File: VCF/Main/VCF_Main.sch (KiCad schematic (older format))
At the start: 51 parts, among them J1 Input, J2 Power, J4 RES_MOD, J5 FREQ_CV, J6 AUDIO_OUT, U1 TL072, U2 TL072, U3 AS3320

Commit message: Update VCF main board for new front panel
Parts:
- removed C1: 15uF, Capacitor_SMD:C_0805_2012Metric, symbol Device:C
- removed C6: 1uF, Capacitor_SMD:C_0805_2012Metric, symbol Device:C
- removed J1: Input, Connector_PinHeader_2.54mm:PinHeader_1x04_P2.54mm_Vertical, symbol Connector_Generic:Conn_01x04
- removed J4: RES_MOD, Connector_PinHeader_2.54mm:PinHeader_1x02_P2.54mm_Vertical, symbol Connector_Generic:Conn_01x02
- removed J5: FREQ_CV, Connector_PinHeader_2.54mm:PinHeader_1x02_P2.54mm_Vertical, symbol Connector_Generic:Conn_01x02
- removed J6: AUDIO_OUT, Connector_PinHeader_2.54mm:PinHeader_1x02_P2.54mm_Vertical, symbol Connector_Generic:Conn_01x02
- removed RV4, RV5: 100K, Connector_PinHeader_2.54mm:PinHeader_1x03_P2.54mm_Vertical, symbol Device:R_POT_US
- added C1: 15uF, Capacitor_SMD:CP_Elec_4x3, symbol Device:CP1
- added C6: 1uF, Capacitor_SMD:CP_Elec_4x3, symbol Device:CP1
- added J1: Power, Connector_PinHeader_2.54mm:PinHeader_1x12_P2.54mm_Vertical, symbol Connector_Generic:Conn_01x12
- C2, C3, C4, C5: footprint AS3320_VCF:Mica_Cap -> Eurorack:Mica_Cap
- R26: footprint AS3320_VCF:Tempco -> Eurorack:Tempco
- U3: symbol AS3320_VCF:AS3320 -> Eurorack:AS3320
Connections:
- net +12V: now also J1.2 (Pin_2)
- net -12V: now also J1.3 (Pin_3)
- net GNDREF: now also J1.1 (Pin_1), J1.12 (Pin_12)
- net at R22.1, U3.10: now also C6.1
- net at R5.2: now also C1.1
- net at R25.2, R27.2: now also C6.2
- net Cutoff_Mod: now reaches R17.2
- net Cutoff_Mod: now also J1.7 (Pin_7)
- net In_1: now reaches R1.2
- net In_1: now also J1.8 (Pin_8)
- net In_2: now reaches R2.2
- net In_2: now also J1.9 (Pin_9)
- net In_3: now reaches R3.2
- net In_3: now also J1.10 (Pin_10)
- net Cutoff: now reaches R15.2
- net Cutoff: now also J1.6 (Pin_6)
- net Res: now reaches R11.2
- net Res: now also J1.4 (Pin_4)
- net Res_Mod: now reaches R12.2
- net Res_Mod: now also J1.5 (Pin_5)
- net at R4.1, U1.7: now also C1.2
- net Out: now reaches R30.1
- net Out: now also J1.11 (Pin_11)
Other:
- moved on the sheet: R1, R12, R3

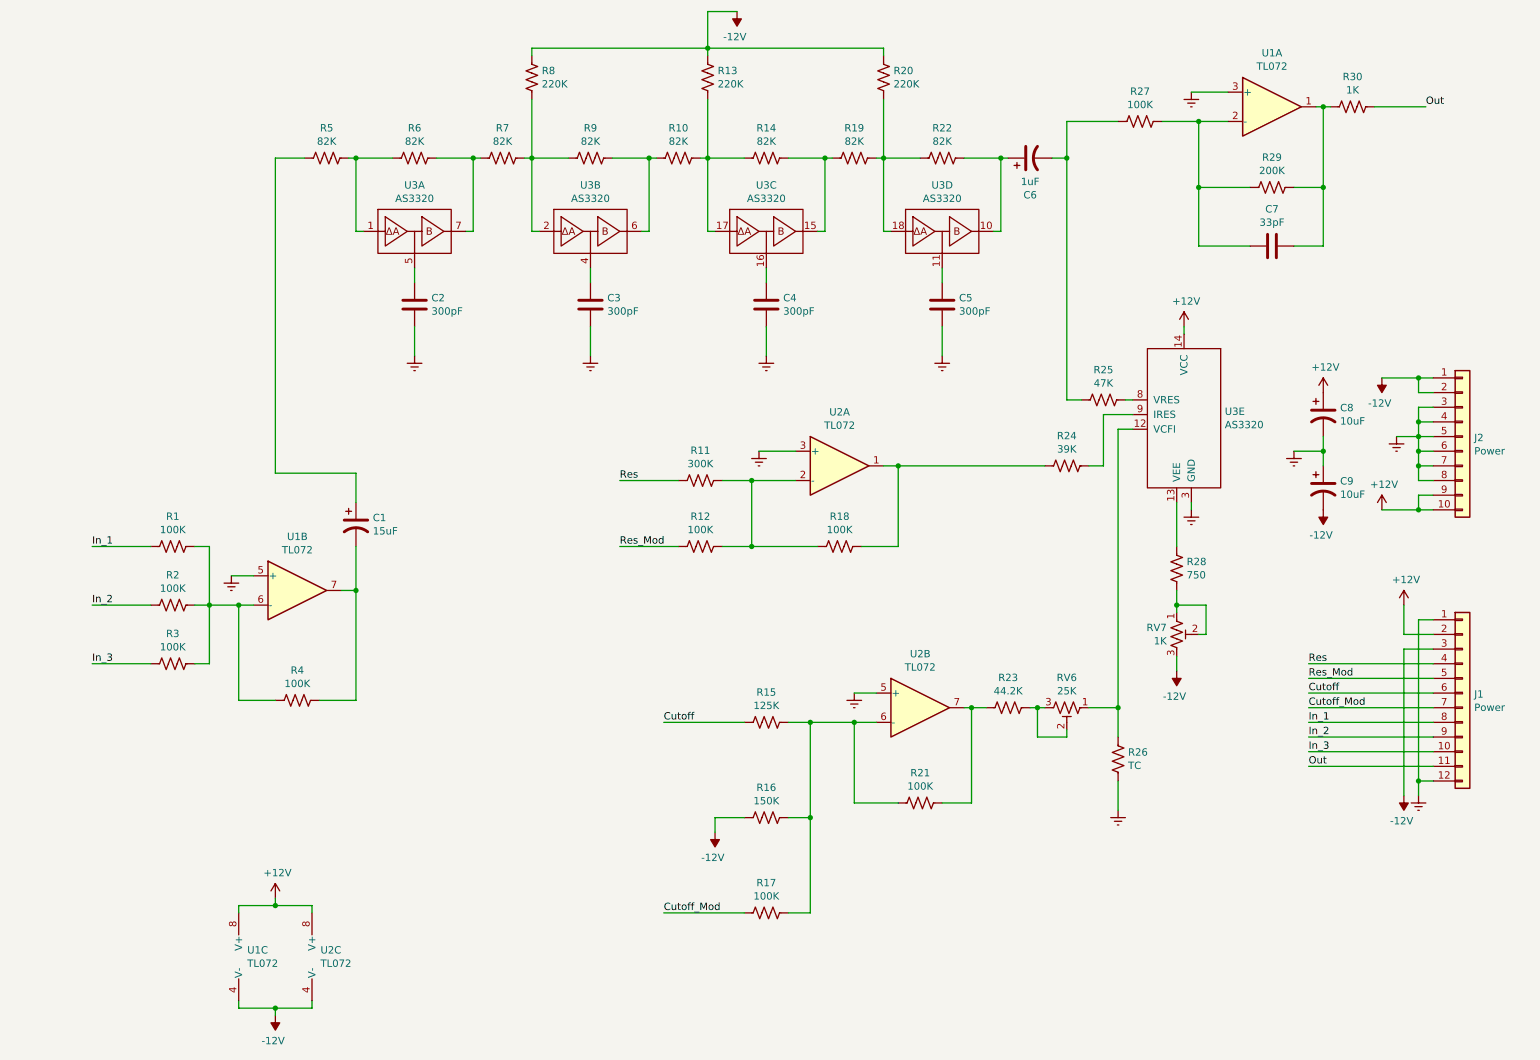
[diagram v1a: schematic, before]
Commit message: Fix inverted resonance control input
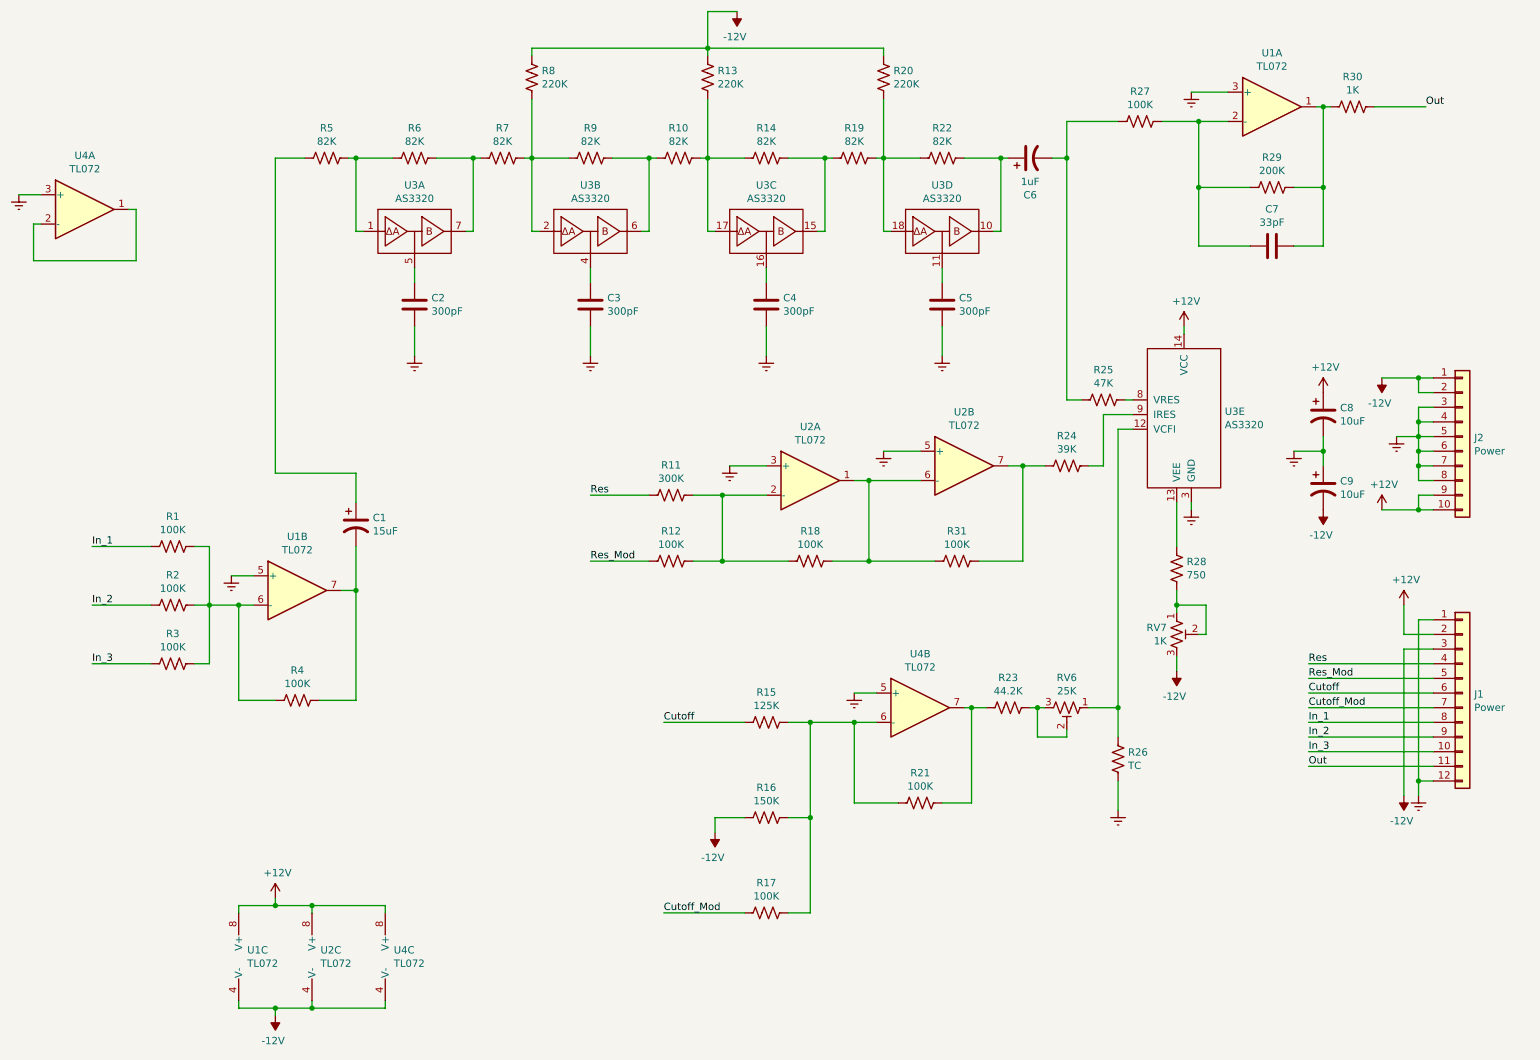
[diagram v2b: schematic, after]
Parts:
- added R31: 100K, Resistor_SMD:R_0805_2012Metric, symbol Device:R_US
- added U4: TL072, Package_DIP:DIP-8_W7.62mm, symbol Amplifier_Operational:TL072
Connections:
- net +12V: now also U4.8 (V+)
- net -12V: now also U4.4 (V-)
- net GNDREF: now also U4.3 (+), U4.5 (+)
- net at R18.1, U2.1: now also U2.6 (-), R31.2; no longer R24.2
- net at R15.1, R16.1, R17.1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: now also U4.6 (-); no longer U2.6 (-)
- net at R21.1, R23.2: now also U4.7; no longer U2.7
- new net: R24.2, R31.1, U2.7
- new net: U4.1, U4.2 (-)
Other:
- moved on the sheet: R11, R12, R18, U2A, U2B
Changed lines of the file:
@@
 L Amplifier_Operational:TL072 U2
 U 1 1 5D5A693C
-P 6450 3650
-F 0 "U2" H 6450 4017 50  0000 C CNN
-F 1 "TL072" H 6450 3926 50  0000 C CNN
-F 2 "Package_DIP:DIP-8_W7.62mm" H 6450 3650 50  0001 C CNN
-F 3 "http://www.ti.com/lit/ds/symlink/tl071.pdf" H 6450 3650 50  0001 C CNN
-	1    6450 3650
+P 6250 3750
+F 0 "U2" H 6250 4117 50  0000 C CNN
+F 1 "TL072" H 6250 4026 50  0000 C CNN
+F 2 "Package_DIP:DIP-8_W7.62mm" H 6250 3750 50  0001 C CNN
+F 3 "http://www.ti.com/lit/ds/symlink/tl071.pdf" H 6250 3750 50  0001 C CNN
+	1    6250 3750
 	1    0    0    -1
 $EndComp
@@
 L Amplifier_Operational:TL072 U2
 U 2 1 5D5A8C75
-P 7000 5300
-F 0 "U2" H 7000 5667 50  0000 C CNN
-F 1 "TL072" H 7000 5576 50  0000 C CNN
-F 2 "Package_DIP:DIP-8_W7.62mm" H 7000 5300 50  0001 C CNN
-F 3 "http://www.ti.com/lit/ds/symlink/tl071.pdf" H 7000 5300 50  0001 C CNN
-	2    7000 5300
+P 7300 3650
+F 0 "U2" H 7300 4017 50  0000 C CNN
+F 1 "TL072" H 7300 3926 50  0000 C CNN
+F 2 "Package_DIP:DIP-8_W7.62mm" H 7300 3650 50  0001 C CNN
+F 3 "http://www.ti.com/lit/ds/symlink/tl071.pdf" H 7300 3650 50  0001 C CNN
+	2    7300 3650
 	1    0    0    -1
 $EndComp
@@
 L power:GNDREF #PWR0118
 U 1 1 5D6384AF
-P 5900 3550
-F 0 "#PWR0118" H 5900 3300 50  0001 C CNN
-F 1 "GNDREF" H 5905 3377 50  0001 C CNN
-F 2 "" H 5900 3550 50  0001 C CNN
-F 3 "" H 5900 3550 50  0001 C CNN
-	1    5900 3550
-	1    0    0    -1
-$EndComp
-Wire Wire Line
-	5900 3550 6150 3550
+P 5700 3650
+F 0 "#PWR0118" H 5700 3400 50  0001 C CNN
+F 1 "GNDREF" H 5705 3477 50  0001 C CNN
+F 2 "" H 5700 3650 50  0001 C CNN
+F 3 "" H 5700 3650 50  0001 C CNN
+	1    5700 3650
+	1    0    0    -1
+$EndComp
+Wire Wire Line
+	5700 3650 5950 3650
 $Comp
 L Device:R_US R11
 U 1 1 5D647527
-P 5500 3750
-F 0 "R11" V 5295 3750 50  0000 C CNN
-F 1 "300K" V 5386 3750 50  0000 C CNN
-F 2 "Resistor_SMD:R_0805_2012Metric" V 5540 3740 50  0001 C CNN
-F 3 "~" H 5500 3750 50  0001 C CNN
-	1    5500 3750
+P 5300 3850
+F 0 "R11" V 5095 3850 50  0000 C CNN
+F 1 "300K" V 5186 3850 50  0000 C CNN
+F 2 "Resistor_SMD:R_0805_2012Metric" V 5340 3840 50  0001 C CNN
+F 3 "~" H 5300 3850 50  0001 C CNN
+	1    5300 3850
 	0    1    1    0
 $EndComp
@@
 L Device:R_US R12
 U 1 1 5D647C16
-P 5500 4200
-F 0 "R12" V 5295 4200 50  0000 C CNN
-F 1 "100K" V 5386 4200 50  0000 C CNN
-F 2 "Resistor_SMD:R_0805_2012Metric" V 5540 4190 50  0001 C CNN
-F 3 "~" H 5500 4200 50  0001 C CNN
-	1    5500 4200
+P 5300 4300
+F 0 "R12" V 5095 4300 50  0000 C CNN
+F 1 "100K" V 5186 4300 50  0000 C CNN
+F 2 "Resistor_SMD:R_0805_2012Metric" V 5340 4290 50  0001 C CNN
+F 3 "~" H 5300 4300 50  0001 C CNN
+	1    5300 4300
 	0    1    1    0
 $EndComp
@@
 L Device:R_US R18
 U 1 1 5D6482AE
-P 6450 4200
-F 0 "R18" V 6245 4200 50  0000 C CNN
-F 1 "100K" V 6336 4200 50  0000 C CNN
-F 2 "Resistor_SMD:R_0805_2012Metric" V 6490 4190 50  0001 C CNN
-F 3 "~" H 6450 4200 50  0001 C CNN
-	1    6450 4200
-	0    1    1    0
-$EndComp
-Wire Wire Line
-	4950 3750 5350 3750
-Wire Wire Line
-	5650 3750 5850 3750
-Wire Wire Line
-	4950 4200 5350 4200
-Wire Wire Line
-	5650 4200 5850 4200
-Connection ~ 5850 3750
-Wire Wire Line
-	5850 3750 6150 3750
-Wire Wire Line
-	5850 4200 6300 4200
-Connection ~ 5850 4200
-Wire Wire Line
-	5850 4200 5850 3750
-Wire Wire Line
-	6600 4200 6850 4200
-Wire Wire Line
-	6850 4200 6850 3650
-Wire Wire Line
-	6850 3650 6750 3650
-Connection ~ 6850 3650
+P 6250 4300
+F 0 "R18" V 6045 4300 50  0000 C CNN
+F 1 "100K" V 6136 4300 50  0000 C CNN
+F 2 "Resistor_SMD:R_0805_2012Metric" V 6290 4290 50  0001 C CNN
+F 3 "~" H 6250 4300 50  0001 C CNN
+	1    6250 4300
+	0    1    1    0
+$EndComp
+Wire Wire Line
+	4750 3850 5150 3850
+Wire Wire Line
+	5450 3850 5650 3850
+Wire Wire Line
+	4750 4300 5150 4300
+Wire Wire Line
+	5450 4300 5650 4300
+Connection ~ 5650 3850
+Wire Wire Line
+	5650 3850 5950 3850
+Wire Wire Line
+	5650 4300 6100 4300
+Connection ~ 5650 4300
+Wire Wire Line
+	5650 4300 5650 3850
+Wire Wire Line
+	6400 4300 6650 4300
+Wire Wire Line
+	6650 4300 6650 3750
+Wire Wire Line
+	6650 3750 6550 3750
+Connection ~ 6650 3750
 $Comp
 L Amplifier_Operational:TL072 U1
@@
 Connection ~ 8350 5300
 Wire Wire Line
-	6850 3650 7850 3650
+	6650 3750 7000 3750
 Wire Wire Line
 	2800 1550 2600 1550
@@
 Text Label 1350 5000 0    50   ~ 0
 In_3
-Text Label 4950 3750 0    50   ~ 0
+Text Label 4750 3850 0    50   ~ 0
 Res
-Text Label 4950 4200 0    50   ~ 0
+Text Label 4750 4300 0    50   ~ 0
 Res_Mod
 Text Label 5250 5400 0    50   ~ 0
@@
 	1    0    0    -1
 $EndComp
+$Comp
+L Amplifier_Operational:TL072 U4
+U 1 1 5D8DED88
+P 1300 1900
+F 0 "U4" H 1300 2267 50  0000 C CNN
+F 1 "TL072" H 1300 2176 50  0000 C CNN
+F 2 "Package_DIP:DIP-8_W7.62mm" H 1300 1900 50  0001 C CNN
+F 3 "http://www.ti.com/lit/ds/symlink/tl071.pdf" H 1300 1900 50  0001 C CNN
+	1    1300 1900
+	1    0    0    -1
+$EndComp
+$Comp
+L Amplifier_Operational:TL072 U4
+U 2 1 5D8E0532
+P 7000 5300
+F 0 "U4" H 7000 5667 50  0000 C CNN
+F 1 "TL072" H 7000 5576 50  0000 C CNN
+F 2 "Package_DIP:DIP-8_W7.62mm" H 7000 5300 50  0001 C CNN
+F 3 "http://www.ti.com/lit/ds/symlink/tl071.pdf" H 7000 5300 50  0001 C CNN
+	2    7000 5300
+	1    0    0    -1
+$EndComp
+$Comp
+L Amplifier_Operational:TL072 U4
+U 3 1 5D8E37FF
+P 3450 7000
+F 0 "U4" H 3408 7046 50  0000 L CNN
+F 1 "TL072" H 3408 6955 50  0000 L CNN
+F 2 "Package_DIP:DIP-8_W7.62mm" H 3450 7000 50  0001 C CNN
+F 3 "http://www.ti.com/lit/ds/symlink/tl071.pdf" H 3450 7000 50  0001 C CNN
+	3    3450 7000
+	1    0    0    -1
+$EndComp
+$Comp
+L Device:R_US R31
+U 1 1 5D93C727
+P 7250 4300
+F 0 "R31" V 7045 4300 50  0000 C CNN
+F 1 "100K" V 7136 4300 50  0000 C CNN
+F 2 "Resistor_SMD:R_0805_2012Metric" V 7290 4290 50  0001 C CNN
+F 3 "~" H 7250 4300 50  0001 C CNN
+	1    7250 4300
+	0    1    1    0
+$EndComp
+Wire Wire Line
+	6650 4300 7100 4300
+Connection ~ 6650 4300
+Wire Wire Line
+	7600 3650 7700 3650
+Wire Wire Line
+	7700 3650 7700 4300
+Wire Wire Line
+	7700 4300 7400 4300
+$Comp
+L power:GNDREF #PWR0110
+U 1 1 5D953B55
+P 6750 3550
+F 0 "#PWR0110" H 6750 3300 50  0001 C CNN
+F 1 "GNDREF" H 6755 3377 50  0001 C CNN
+F 2 "" H 6750 3550 50  0001 C CNN
+F 3 "" H 6750 3550 50  0001 C CNN
+	1    6750 3550
+	1    0    0    -1
+$EndComp
+Wire Wire Line
+	6750 3550 7000 3550
+Wire Wire Line
+	7700 3650 7850 3650
+Connection ~ 7700 3650
+$Comp
+L power:GNDREF #PWR0111
+U 1 1 5D9ABD29
+P 850 1800
+F 0 "#PWR0111" H 850 1550 50  0001 C CNN
+F 1 "GNDREF" H 855 1627 50  0001 C CNN
+F 2 "" H 850 1800 50  0001 C CNN
+F 3 "" H 850 1800 50  0001 C CNN
+	1    850  1800
+	1    0    0    -1
+$EndComp
+Wire Wire Line
+	850  1800 1000 1800
+Wire Wire Line
+	1000 2000 950  2000
+Wire Wire Line
+	950  2000 950  2250
+Wire Wire Line
+	950  2250 1650 2250
+Wire Wire Line
+	1650 2250 1650 1900
+Wire Wire Line
+	1650 1900 1600 1900
+Wire Wire Line
+	2850 6650 3350 6650
+Wire Wire Line
+	3350 6650 3350 6700
+Connection ~ 2850 6650
+Wire Wire Line
+	2850 7350 3350 7350
+Wire Wire Line
+	3350 7350 3350 7300
+Connection ~ 2850 7350
 $EndSCHEMATC

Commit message: Bunch of bug fixes and tweaks
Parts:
- added C10, C11, C12, C13: C, Capacitor_SMD:C_0805_2012Metric, symbol Device:C
- added H1: Top_MH1, Eurorack:eurorack_mounting_hole, symbol Mechanical:MountingHole_Pad
- added H2: Bottom_MH1, Eurorack:eurorack_mounting_hole, symbol Mechanical:MountingHole_Pad
- added H3: Top_MH2, Eurorack:eurorack_mounting_hole, symbol Mechanical:MountingHole_Pad
- added H4: Bottom_MH2, Eurorack:eurorack_mounting_hole, symbol Mechanical:MountingHole_Pad
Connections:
- net GNDREF: now also H1.1, H2.1, H3.1, H4.1
- net at R24.2, R31.1, U2.7: now also C13.2
- net at R15.1, R16.1, R17.1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: now also C12.1
- net at R21.1, R23.2, U4.7: now also C12.2
- net at R18.1, R31.2, U2.1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: now also C11.2, C13.1
- net at R11.1, R12.1, R18.2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: now also C11.1
- net at R1.1, R2.1, R3.1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: now also C10.1
- net at C1.2, R4.1, U1.7: now also C10.2
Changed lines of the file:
@@
 	3350 7350 3350 7300
 Connection ~ 2850 7350
+$Comp
+L Device:C C10
+U 1 1 5D939BB0
+P 2750 5700
+F 0 "C10" V 3002 5700 50  0000 C CNN
+F 1 "C" V 2911 5700 50  0000 C CNN
+F 2 "Capacitor_SMD:C_0805_2012Metric" H 2788 5550 50  0001 C CNN
+F 3 "~" H 2750 5700 50  0001 C CNN
+	1    2750 5700
+	0    -1   -1   0
+$EndComp
+Wire Wire Line
+	2350 5250 2350 5700
+Wire Wire Line
+	2350 5700 2600 5700
+Connection ~ 2350 5250
+Wire Wire Line
+	3150 5250 3150 5700
+Wire Wire Line
+	3150 5700 2900 5700
+Connection ~ 3150 5250
+$Comp
+L Device:C C11
+U 1 1 5D954A6E
+P 6250 4750
+F 0 "C11" V 6502 4750 50  0000 C CNN
+F 1 "C" V 6411 4750 50  0000 C CNN
+F 2 "Capacitor_SMD:C_0805_2012Metric" H 6288 4600 50  0001 C CNN
+F 3 "~" H 6250 4750 50  0001 C CNN
+	1    6250 4750
+	0    -1   -1   0
+$EndComp
+Wire Wire Line
+	5650 4300 5650 4750
+Wire Wire Line
+	5650 4750 6100 4750
+Wire Wire Line
+	6400 4750 6650 4750
+Wire Wire Line
+	6650 4750 6650 4300
+$Comp
+L Device:C C13
+U 1 1 5D970860
+P 7250 4750
+F 0 "C13" V 7502 4750 50  0000 C CNN
+F 1 "C" V 7411 4750 50  0000 C CNN
+F 2 "Capacitor_SMD:C_0805_2012Metric" H 7288 4600 50  0001 C CNN
+F 3 "~" H 7250 4750 50  0001 C CNN
+	1    7250 4750
+	0    -1   -1   0
+$EndComp
+Wire Wire Line
+	6650 4750 7100 4750
+Connection ~ 6650 4750
+Wire Wire Line
+	7400 4750 7700 4750
+Wire Wire Line
+	7700 4750 7700 4300
+Connection ~ 7700 4300
+$Comp
+L Device:C C12
+U 1 1 5D98CF1C
+P 7000 6350
+F 0 "C12" V 7252 6350 50  0000 C CNN
+F 1 "C" V 7161 6350 50  0000 C CNN
+F 2 "Capacitor_SMD:C_0805_2012Metric" H 7038 6200 50  0001 C CNN
+F 3 "~" H 7000 6350 50  0001 C CNN
+	1    7000 6350
+	0    -1   -1   0
+$EndComp
+Wire Wire Line
+	6850 6350 6550 6350
+Wire Wire Line
+	6550 6350 6550 5950
+Connection ~ 6550 5950
+Wire Wire Line
+	7150 6350 7350 6350
+Wire Wire Line
+	7350 6350 7350 5950
+Connection ~ 7350 5950
+$Comp
+L Mechanical:MountingHole_Pad H1
+U 1 1 5D9AC4F4
+P 1050 700
+F 0 "H1" H 1150 749 50  0000 L CNN
+F 1 "Top_MH1" H 1150 658 50  0000 L CNN
+F 2 "Eurorack:eurorack_mounting_hole" H 1050 700 50  0001 C CNN
+F 3 "~" H 1050 700 50  0001 C CNN
+	1    1050 700
+	1    0    0    -1
+$EndComp
+$Comp
+L power:GNDREF #PWR0114
+U 1 1 5D9AD073
+P 1050 800
+F 0 "#PWR0114" H 1050 550 50  0001 C CNN
+F 1 "GNDREF" H 1055 627 50  0001 C CNN
+F 2 "" H 1050 800 50  0001 C CNN
+F 3 "" H 1050 800 50  0001 C CNN
+	1    1050 800
+	1    0    0    -1
+$EndComp
+$Comp
+L Mechanical:MountingHole_Pad H3
+U 1 1 5D9AE4DC
+P 1900 700
+F 0 "H3" H 2000 749 50  0000 L CNN
+F 1 "Top_MH2" H 2000 658 50  0000 L CNN
+F 2 "Eurorack:eurorack_mounting_hole" H 1900 700 50  0001 C CNN
+F 3 "~" H 1900 700 50  0001 C CNN
+	1    1900 700
+	1    0    0    -1
+$EndComp
+$Comp
+L power:GNDREF #PWR0115
+U 1 1 5D9AE4E2
+P 1900 800
+F 0 "#PWR0115" H 1900 550 50  0001 C CNN
+F 1 "GNDREF" H 1905 627 50  0001 C CNN
+F 2 "" H 1900 800 50  0001 C CNN
+F 3 "" H 1900 800 50  0001 C CNN
+	1    1900 800
+	1    0    0    -1
+$EndComp
+$Comp
+L Mechanical:MountingHole_Pad H2
+U 1 1 5D9BC519
+P 1050 1100
+F 0 "H2" H 1150 1149 50  0000 L CNN
+F 1 "Bottom_MH1" H 1150 1058 50  0000 L CNN
+F 2 "Eurorack:eurorack_mounting_hole" H 1050 1100 50  0001 C CNN
+F 3 "~" H 1050 1100 50  0001 C CNN
+	1    1050 1100
+	1    0    0    -1
+$EndComp
+$Comp
+L power:GNDREF #PWR0116
+U 1 1 5D9BC51F
+P 1050 1200
+F 0 "#PWR0116" H 1050 950 50  0001 C CNN
+F 1 "GNDREF" H 1055 1027 50  0001 C CNN
+F 2 "" H 1050 1200 50  0001 C CNN
+F 3 "" H 1050 1200 50  0001 C CNN
+	1    1050 1200
+	1    0    0    -1
+$EndComp
+$Comp
+L Mechanical:MountingHole_Pad H4
+U 1 1 5D9CA89E
+P 1900 1100
+F 0 "H4" H 2000 1149 50  0000 L CNN
+F 1 "Bottom_MH2" H 2000 1058 50  0000 L CNN
+F 2 "Eurorack:eurorack_mounting_hole" H 1900 1100 50  0001 C CNN
+F 3 "~" H 1900 1100 50  0001 C CNN
+	1    1900 1100
+	1    0    0    -1
+$EndComp
+$Comp
+L power:GNDREF #PWR0117
+U 1 1 5D9CA8A4
+P 1900 1200
+F 0 "#PWR0117" H 1900 950 50  0001 C CNN
+F 1 "GNDREF" H 1905 1027 50  0001 C CNN
+F 2 "" H 1900 1200 50  0001 C CNN
+F 3 "" H 1900 1200 50  0001 C CNN
+	1    1900 1200
+	1    0    0    -1
+$EndComp
 $EndSCHEMATC
